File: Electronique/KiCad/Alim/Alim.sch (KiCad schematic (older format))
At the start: 19 parts, among them P1 CONN_2, P2 CONN_2, P3 CONN_2, T1 MMBT2907A, T2 MMBT2907A, T3 NJVMJD44H11, T4 NJVMJD44H11

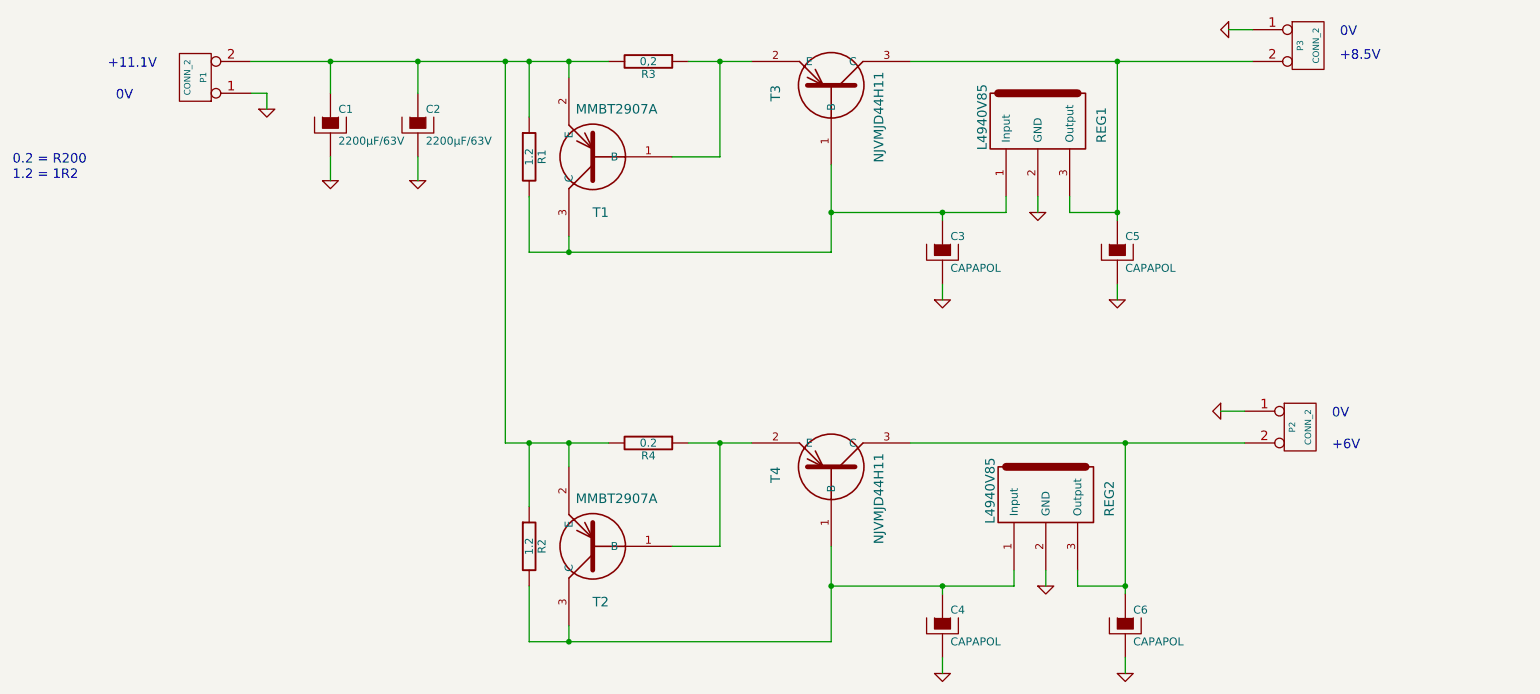
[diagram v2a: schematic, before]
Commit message: Modification de la partie alimentation. Ajout de la partie Module Mini Alim qui est un régulateur monté pour être plugé et déplugé sur la carte mère alimentation à revoir totalement. Ce procédé permet de faire des tests en dehors de la carte principale.
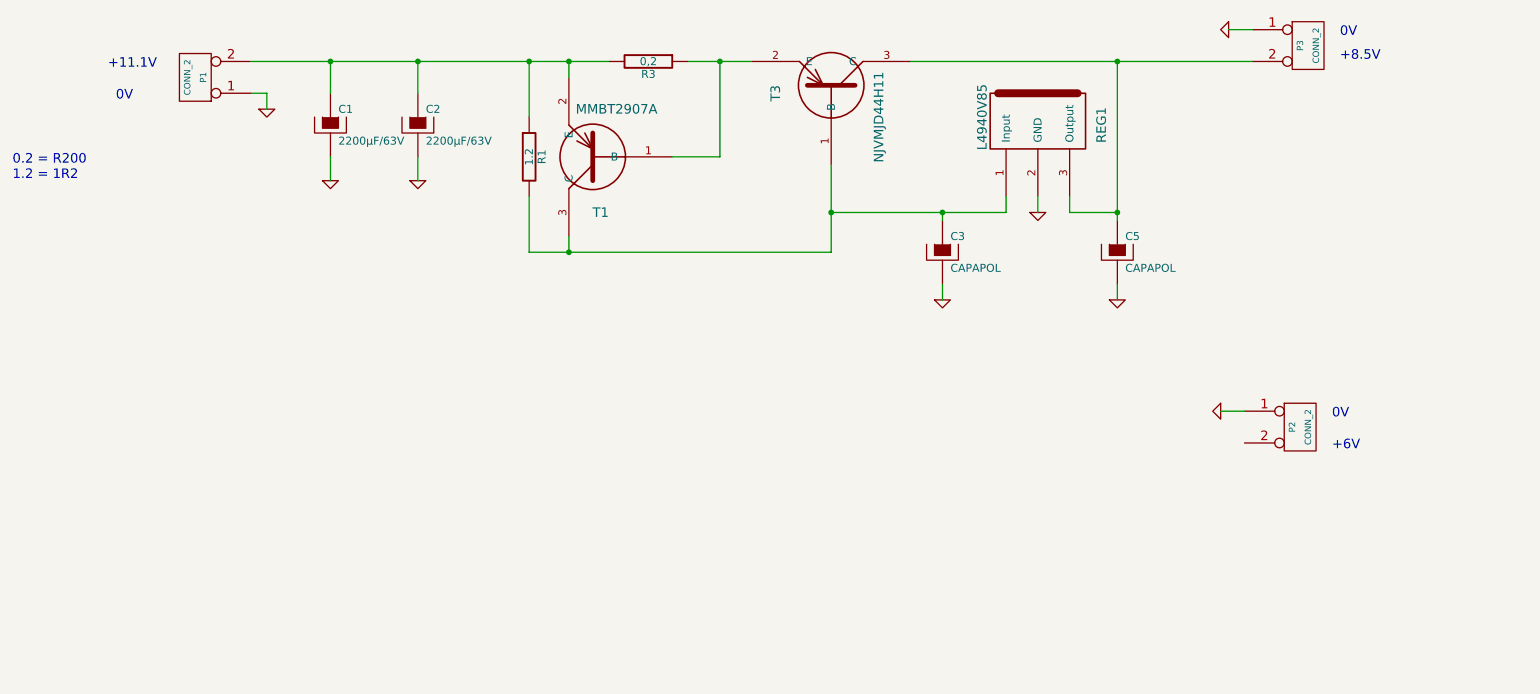
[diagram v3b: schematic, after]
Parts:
- removed C4, C6: CAPAPOL, symbol CAPAPOL
- removed R2: 1.2, symbol R
- removed R4: 0.2, symbol R
- removed REG2: L4940V85, symbol L4940V85
- removed T2: MMBT2907A, symbol MMBT2907A
- removed T4: NJVMJD44H11, symbol NJVMJD44H11
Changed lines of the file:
@@
-EESchema Schematic File Version 2  date sam. 27 sept. 2014 09:30:36 CEST
+EESchema Schematic File Version 2  date mar. 04 nov. 2014 14:59:27 CET
 LIBS:power
 LIBS:device
@@
 Sheet 1 1
 Title ""
-Date "27 sep 2014"
+Date "4 nov 2014"
 Rev ""
 Comp ""
@@
 	2550 1900 2450 1900
 Wire Wire Line
-	8700 4100 6600 4100
-Wire Wire Line
 	8750 1700 6600 1700
-Wire Wire Line
-	6800 5550 6800 5450
-Connection ~ 6100 5000
-Wire Wire Line
-	6100 5000 7250 5000
-Wire Wire Line
-	7250 5000 7250 4900
-Connection ~ 7950 5000
-Wire Wire Line
-	7950 5000 7650 5000
-Wire Wire Line
-	7650 5000 7650 4900
-Wire Wire Line
-	7950 5550 7950 5450
-Connection ~ 7950 4100
-Connection ~ 4450 5350
-Wire Wire Line
-	4450 5250 4450 5350
-Wire Wire Line
-	5200 4100 5600 4100
-Connection ~ 4450 4100
-Wire Wire Line
-	4450 4100 4450 4250
-Connection ~ 4050 1700
-Wire Wire Line
-	4700 4100 4050 4100
-Wire Wire Line
-	4050 4100 4050 1700
 Wire Wire Line
 	6800 3200 6800 3100
@@
 Wire Wire Line
 	7900 3200 7900 3100
-Wire Wire Line
-	4200 4100 4200 4500
-Connection ~ 4200 4100
-Wire Wire Line
-	4200 5000 4200 5350
-Wire Wire Line
-	4200 5350 6100 5350
-Wire Wire Line
-	6100 5350 6100 4750
-Wire Wire Line
-	5400 4100 5400 4750
-Wire Wire Line
-	5400 4750 5100 4750
-Connection ~ 5400 4100
-Wire Wire Line
-	7950 4100 7950 5050
-Wire Wire Line
-	7450 4900 7450 5000
-Wire Wire Line
-	6800 5050 6800 5000
-Connection ~ 6800 5000
 Wire Wire Line
 	8750 1500 8600 1500
@@
 +11.1V
 $Comp
-L GND #PWR02
-U 1 1 542149E6
-P 6800 5550
-F 0 "#PWR02" H 6800 5550 30  0001 C CNN
-F 1 "GND" H 6800 5480 30  0001 C CNN
-	1    6800 5550
-	1    0    0    -1
-$EndComp
-$Comp
-L GND #PWR03
-U 1 1 542149E4
-P 7950 5550
-F 0 "#PWR03" H 7950 5550 30  0001 C CNN
-F 1 "GND" H 7950 5480 30  0001 C CNN
-	1    7950 5550
-	1    0    0    -1
-$EndComp
-$Comp
-L GND #PWR04
-U 1 1 542149E1
-P 7450 5000
-F 0 "#PWR04" H 7450 5000 30  0001 C CNN
-F 1 "GND" H 7450 4930 30  0001 C CNN
-	1    7450 5000
-	1    0    0    -1
-$EndComp
-$Comp
 L GND #PWR05
 U 1 1 542149DE
@@
 $EndComp
 $Comp
-L L4940V85 REG2
-U 1 1 5421499A
-P 7450 4600
-F 0 "REG2" V 7850 4750 60  0000 C CNN
-F 1 "L4940V85" V 7100 4800 60  0000 C CNN
-	1    7450 4600
-	1    0    0    -1
-$EndComp
-$Comp
 L L4940V85 REG1
 U 1 1 54214989
@@
 $EndComp
 $Comp
-L CAPAPOL C6
-U 1 1 54214981
-P 7950 5250
-F 0 "C6" H 8000 5350 50  0000 L CNN
-F 1 "CAPAPOL" H 8000 5150 50  0000 L CNN
-	1    7950 5250
-	1    0    0    -1
-$EndComp
-$Comp
-L CAPAPOL C4
-U 1 1 5421497E
-P 6800 5250
-F 0 "C4" H 6850 5350 50  0000 L CNN
-F 1 "CAPAPOL" H 6850 5150 50  0000 L CNN
-	1    6800 5250
-	1    0    0    -1
-$EndComp
-$Comp
 L CAPAPOL C5
 U 1 1 5421497B
@@
 $EndComp
 $Comp
-L NJVMJD44H11 T4
-U 1 1 54214937
-P 6100 4250
-F 0 "T4" H 6150 3900 60  0000 C CNN
-F 1 "NJVMJD44H11" H 6300 4550 60  0000 C CNN
-	1    6100 4250
-	0    1    1    0
-$EndComp
-$Comp
 L NJVMJD44H11 T3
 U 1 1 54214931
@@
 $EndComp
 $Comp
-L R R4
-U 1 1 54214917
-P 4950 4100
-F 0 "R4" V 5030 4100 50  0000 C CNN
-F 1 "0.2" V 4950 4100 50  0000 C CNN
-	1    4950 4100
-	0    1    1    0
-$EndComp
-$Comp
 L R R3
 U 1 1 5421490C
@@
 $EndComp
 $Comp
-L R R2
-U 1 1 54214907
-P 4200 4750
-F 0 "R2" V 4280 4750 50  0000 C CNN
-F 1 "1.2" V 4200 4750 50  0000 C CNN
-	1    4200 4750
-	1    0    0    -1
-$EndComp
-$Comp
 L R R1
 U 1 1 54214900
@@
 	1    0    0    -1
 $EndComp
-$Comp
-L MMBT2907A T2
-U 1 1 542148F7
-P 4600 4750
-F 0 "T2" H 4650 4400 60  0000 C CNN
-F 1 "MMBT2907A" H 4750 5050 60  0000 C CNN
-	1    4600 4750
-	1    0    0    -1
-$EndComp

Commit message: Modification du PCB alimentation
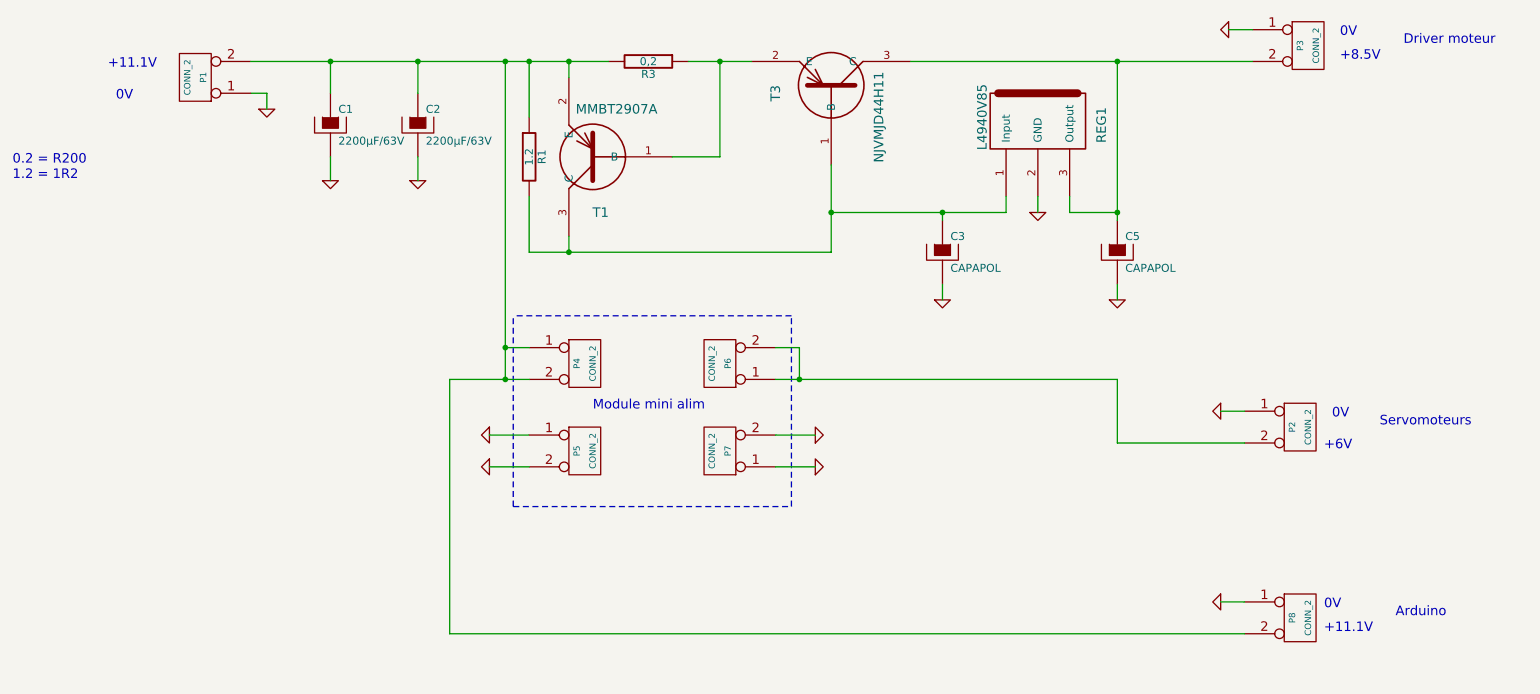
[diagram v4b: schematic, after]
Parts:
- added P4, P5, P6, P7, P8: CONN_2, symbol CONN_2
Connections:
- net GND: now also P5.1 (P1), P5.2 (PM), P7.1 (P1), P7.2 (PM), P8.1 (P1)
- net at C1.1, C2.1, P1.2 (PM)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: now also P4.1 (P1), P4.2 (PM), P8.2 (PM)
- net at P2.2 (PM): now also P6.1 (P1), P6.2 (PM)
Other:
- note added: "Arduino"
- note added: "Driver moteur"
- note added: "Module mini alim"
- note added: "Servomoteurs"
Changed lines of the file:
@@
-EESchema Schematic File Version 2  date mar. 04 nov. 2014 14:59:27 CET
+EESchema Schematic File Version 2  date dim. 14 déc. 2014 23:07:17 CET
 LIBS:power
 LIBS:device
@@
 Sheet 1 1
 Title ""
-Date "4 nov 2014"
+Date "14 dec 2014"
 Rev ""
 Comp ""
@@
 Comment4 ""
 $EndDescr
+Connection ~ 4050 3700
+Wire Wire Line
+	8700 5300 3700 5300
+Wire Wire Line
+	3700 5300 3700 3700
+Wire Wire Line
+	3700 3700 4200 3700
+Wire Wire Line
+	5750 4250 6000 4250
+Wire Wire Line
+	3950 4250 4200 4250
+Connection ~ 5900 3700
+Wire Wire Line
+	8700 4100 7900 4100
+Wire Wire Line
+	7900 4100 7900 3700
+Wire Wire Line
+	7900 3700 5750 3700
+Connection ~ 4050 3500
+Wire Wire Line
+	4050 3700 4050 1700
+Wire Notes Line
+	4100 4500 4100 3300
+Wire Notes Line
+	4100 4500 5850 4500
+Wire Notes Line
+	5850 4500 5850 3300
+Wire Notes Line
+	5850 3300 4100 3300
+Wire Wire Line
+	2950 2300 2950 2450
+Connection ~ 2950 1700
+Wire Wire Line
+	2950 1900 2950 1700
+Wire Wire Line
+	4700 1700 2450 1700
+Wire Wire Line
+	8700 3900 8550 3900
+Wire Wire Line
+	8750 1500 8600 1500
+Wire Wire Line
+	7900 3200 7900 3100
+Connection ~ 6800 2650
+Connection ~ 6100 2650
+Wire Wire Line
+	6100 2650 7200 2650
+Wire Wire Line
+	7400 2650 7400 2550
+Wire Wire Line
+	7900 2700 7900 1700
+Wire Wire Line
+	5600 1700 5200 1700
+Wire Wire Line
+	6100 2350 6100 2900
+Wire Wire Line
+	6100 2900 4200 2900
+Wire Wire Line
+	4200 2900 4200 2550
+Wire Wire Line
+	4450 1800 4450 1700
+Connection ~ 4450 1700
+Wire Wire Line
+	4200 1700 4200 2050
+Connection ~ 4200 1700
+Wire Wire Line
+	4450 2800 4450 2900
+Connection ~ 4450 2900
+Wire Wire Line
+	5400 1700 5400 2300
+Wire Wire Line
+	5400 2300 5100 2300
+Connection ~ 5400 1700
+Connection ~ 7900 1700
+Wire Wire Line
+	7600 2550 7600 2650
+Wire Wire Line
+	7600 2650 7900 2650
+Connection ~ 7900 2650
+Wire Wire Line
+	7200 2650 7200 2550
+Wire Wire Line
+	6800 2700 6800 2650
+Wire Wire Line
+	6800 3200 6800 3100
+Wire Wire Line
+	6600 1700 8750 1700
+Wire Wire Line
+	2450 1900 2550 1900
+Wire Wire Line
+	2550 1900 2550 2000
+Wire Wire Line
+	3500 1700 3500 1900
+Connection ~ 3500 1700
 Wire Wire Line
 	3500 2300 3500 2450
-Connection ~ 3500 1700
-Wire Wire Line
-	3500 1900 3500 1700
-Wire Wire Line
-	2550 2000 2550 1900
-Wire Wire Line
-	2550 1900 2450 1900
-Wire Wire Line
-	8750 1700 6600 1700
-Wire Wire Line
-	6800 3200 6800 3100
-Wire Wire Line
-	6800 2650 6800 2700
-Wire Wire Line
-	7200 2550 7200 2650
-Connection ~ 7900 2650
-Wire Wire Line
-	7900 2650 7600 2650
-Wire Wire Line
-	7600 2650 7600 2550
-Connection ~ 7900 1700
-Connection ~ 5400 1700
-Wire Wire Line
-	5100 2300 5400 2300
-Wire Wire Line
-	5400 2300 5400 1700
-Connection ~ 4450 2900
-Wire Wire Line
-	4450 2800 4450 2900
-Connection ~ 4200 1700
-Wire Wire Line
-	4200 2050 4200 1700
-Connection ~ 4450 1700
-Wire Wire Line
-	4450 1800 4450 1700
-Wire Wire Line
-	4200 2550 4200 2900
-Wire Wire Line
-	4200 2900 6100 2900
-Wire Wire Line
-	6100 2900 6100 2350
-Wire Wire Line
-	5200 1700 5600 1700
-Wire Wire Line
-	7900 1700 7900 2700
-Wire Wire Line
-	7400 2650 7400 2550
-Wire Wire Line
-	7200 2650 6100 2650
-Connection ~ 6100 2650
-Connection ~ 6800 2650
-Wire Wire Line
-	7900 3200 7900 3100
-Wire Wire Line
-	8750 1500 8600 1500
-Wire Wire Line
-	8700 3900 8550 3900
-Wire Wire Line
-	2450 1700 4700 1700
-Wire Wire Line
-	2950 1900 2950 1700
-Connection ~ 2950 1700
-Wire Wire Line
-	2950 2300 2950 2450
+Wire Wire Line
+	4050 3500 4200 3500
+Connection ~ 4050 1700
+Wire Wire Line
+	5750 3500 5900 3500
+Wire Wire Line
+	5900 3500 5900 3700
+Wire Wire Line
+	3950 4050 4200 4050
+Wire Wire Line
+	5750 4050 6000 4050
+Wire Wire Line
+	8700 5100 8550 5100
+Text Notes 9700 1600 0    60   ~ 0
+Driver moteur
+Text Notes 9550 4000 0    60   ~ 0
+Servomoteurs
+Text Notes 9650 5200 0    60   ~ 0
+Arduino
+Text Notes 9200 5150 0    60   ~ 0
+0V
+Text Notes 9200 5300 0    60   ~ 0
++11.1V
 $Comp
 L GND #PWR01
+U 1 1 548DFEE8
+P 8550 5100
+F 0 "#PWR01" H 8550 5100 30  0001 C CNN
+F 1 "GND" H 8550 5030 30  0001 C CNN
+	1    8550 5100
+	0    1    1    0
+$EndComp
+$Comp
+L CONN_2 P8
+U 1 1 548DFEDA
+P 9050 5200
+F 0 "P8" V 9000 5200 40  0000 C CNN
+F 1 "CONN_2" V 9100 5200 40  0000 C CNN
+	1    9050 5200
+	1    0    0    -1
+$EndComp
+$Comp
+L GND #PWR02
+U 1 1 548DFE9E
+P 6000 4250
+F 0 "#PWR02" H 6000 4250 30  0001 C CNN
+F 1 "GND" H 6000 4180 30  0001 C CNN
+	1    6000 4250
+	0    -1   -1   0
+$EndComp
+$Comp
+L GND #PWR03
+U 1 1 548DFE98
+P 6000 4050
+F 0 "#PWR03" H 6000 4050 30  0001 C CNN
+F 1 "GND" H 6000 3980 30  0001 C CNN
+	1    6000 4050
+	0    -1   -1   0
+$EndComp
+$Comp
+L GND #PWR04
+U 1 1 548DFE92
+P 3950 4250
+F 0 "#PWR04" H 3950 4250 30  0001 C CNN
+F 1 "GND" H 3950 4180 30  0001 C CNN
+	1    3950 4250
+	0    1    1    0
+$EndComp
+$Comp
+L GND #PWR05
+U 1 1 548DFE8A
+P 3950 4050
+F 0 "#PWR05" H 3950 4050 30  0001 C CNN
+F 1 "GND" H 3950 3980 30  0001 C CNN
+	1    3950 4050
+	0    1    1    0
+$EndComp
+Text Notes 4600 3900 0    60   ~ 0
+Module mini alim
+$Comp
+L CONN_2 P7
+U 1 1 548DFE26
+P 5400 4150
+F 0 "P7" V 5350 4150 40  0000 C CNN
+F 1 "CONN_2" V 5450 4150 40  0000 C CNN
+	1    5400 4150
+	-1   0    0    1
+$EndComp
+$Comp
+L CONN_2 P6
+U 1 1 548DFE22
+P 5400 3600
+F 0 "P6" V 5350 3600 40  0000 C CNN
+F 1 "CONN_2" V 5450 3600 40  0000 C CNN
+	1    5400 3600
+	-1   0    0    1
+$EndComp
+$Comp
+L CONN_2 P5
+U 1 1 548DFE1E
+P 4550 4150
+F 0 "P5" V 4500 4150 40  0000 C CNN
+F 1 "CONN_2" V 4600 4150 40  0000 C CNN
+	1    4550 4150
+	1    0    0    -1
+$EndComp
+$Comp
+L CONN_2 P4
+U 1 1 548DFE1A
+P 4550 3600
+F 0 "P4" V 4500 3600 40  0000 C CNN
+F 1 "CONN_2" V 4600 3600 40  0000 C CNN
+	1    4550 3600
+	1    0    0    -1
+$EndComp
+$Comp
+L GND #PWR06
 U 1 1 5426672A
 P 2950 2450
-F 0 "#PWR01" H 2950 2450 30  0001 C CNN
+F 0 "#PWR06" H 2950 2450 30  0001 C CNN
 F 1 "GND" H 2950 2380 30  0001 C CNN
 	1    2950 2450
@@
 Text Notes 950  2450 0    60   ~ 0
 0.2 = R200\n1.2 = 1R2
-Text Notes 9250 4150 0    60   ~ 0
+Text Notes 9200 4150 0    60   ~ 0
 +6V
 Text Notes 9250 3950 0    60   ~ 0
@@
 +11.1V
 $Comp
-L GND #PWR05
+L GND #PWR07
 U 1 1 542149DE
 P 8550 3900
-F 0 "#PWR05" H 8550 3900 30  0001 C CNN
+F 0 "#PWR07" H 8550 3900 30  0001 C CNN
 F 1 "GND" H 8550 3830 30  0001 C CNN
 	1    8550 3900
@@
 $EndComp
 $Comp
-L GND #PWR06
+L GND #PWR08
 U 1 1 542149DA
 P 8600 1500
-F 0 "#PWR06" H 8600 1500 30  0001 C CNN
+F 0 "#PWR08" H 8600 1500 30  0001 C CNN
 F 1 "GND" H 8600 1430 30  0001 C CNN
 	1    8600 1500
@@
 $EndComp
 $Comp
-L GND #PWR07
+L GND #PWR09
 U 1 1 542149D6
 P 7900 3200
-F 0 "#PWR07" H 7900 3200 30  0001 C CNN
+F 0 "#PWR09" H 7900 3200 30  0001 C CNN
 F 1 "GND" H 7900 3130 30  0001 C CNN
 	1    7900 3200
@@
 $EndComp
 $Comp
-L GND #PWR08
+L GND #PWR010
 U 1 1 542149D3
 P 6800 3200
-F 0 "#PWR08" H 6800 3200 30  0001 C CNN
+F 0 "#PWR010" H 6800 3200 30  0001 C CNN
 F 1 "GND" H 6800 3130 30  0001 C CNN
 	1    6800 3200
@@
 $EndComp
 $Comp
-L GND #PWR09
+L GND #PWR011
 U 1 1 542149CF
 P 7400 2650
-F 0 "#PWR09" H 7400 2650 30  0001 C CNN
+F 0 "#PWR011" H 7400 2650 30  0001 C CNN
 F 1 "GND" H 7400 2580 30  0001 C CNN
 	1    7400 2650
@@
 $EndComp
 $Comp
-L GND #PWR010
+L GND #PWR012
 U 1 1 542149CA
 P 3500 2450
-F 0 "#PWR010" H 3500 2450 30  0001 C CNN
+F 0 "#PWR012" H 3500 2450 30  0001 C CNN
 F 1 "GND" H 3500 2380 30  0001 C CNN
 	1    3500 2450
@@
 $EndComp
 $Comp
-L GND #PWR011
+L GND #PWR013
 U 1 1 542149C5
 P 2550 2000
-F 0 "#PWR011" H 2550 2000 30  0001 C CNN
+F 0 "#PWR013" H 2550 2000 30  0001 C CNN
 F 1 "GND" H 2550 1930 30  0001 C CNN
 	1    2550 2000

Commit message: Modification du PCB alimentation
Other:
- note added: "+5V"
- note removed: "+6V"
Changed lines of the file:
@@
-EESchema Schematic File Version 2  date dim. 14 déc. 2014 23:07:17 CET
+EESchema Schematic File Version 2  date lun. 15 déc. 2014 09:16:07 CET
 LIBS:power
 LIBS:device
@@
 Sheet 1 1
 Title ""
-Date "14 dec 2014"
+Date "15 dec 2014"
 Rev ""
 Comp ""
@@
 0.2 = R200\n1.2 = 1R2
 Text Notes 9200 4150 0    60   ~ 0
-+6V
++5V
 Text Notes 9250 3950 0    60   ~ 0
 0V

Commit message: Modification du schéma au niveau de C3 et C5 **Mise en place de la bonne valeur**
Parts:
- C3, C5: value CAPAPOL -> 1µF
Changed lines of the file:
@@
-EESchema Schematic File Version 2  date lun. 15 déc. 2014 09:16:07 CET
+EESchema Schematic File Version 2  date lun. 15 déc. 2014 23:51:44 CET
 LIBS:power
 LIBS:device
@@
 P 7900 2900
 F 0 "C5" H 7950 3000 50  0000 L CNN
-F 1 "CAPAPOL" H 7950 2800 50  0000 L CNN
+F 1 "1µF" H 7950 2800 50  0000 L CNN
 	1    7900 2900
 	1    0    0    -1
@@
 P 6800 2900
 F 0 "C3" H 6850 3000 50  0000 L CNN
-F 1 "CAPAPOL" H 6850 2800 50  0000 L CNN
+F 1 "1µF" H 6850 2800 50  0000 L CNN
 	1    6800 2900
 	1    0    0    -1
